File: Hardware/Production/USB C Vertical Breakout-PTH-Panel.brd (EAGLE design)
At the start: 106.7 x 103.4 mm, 586 parts

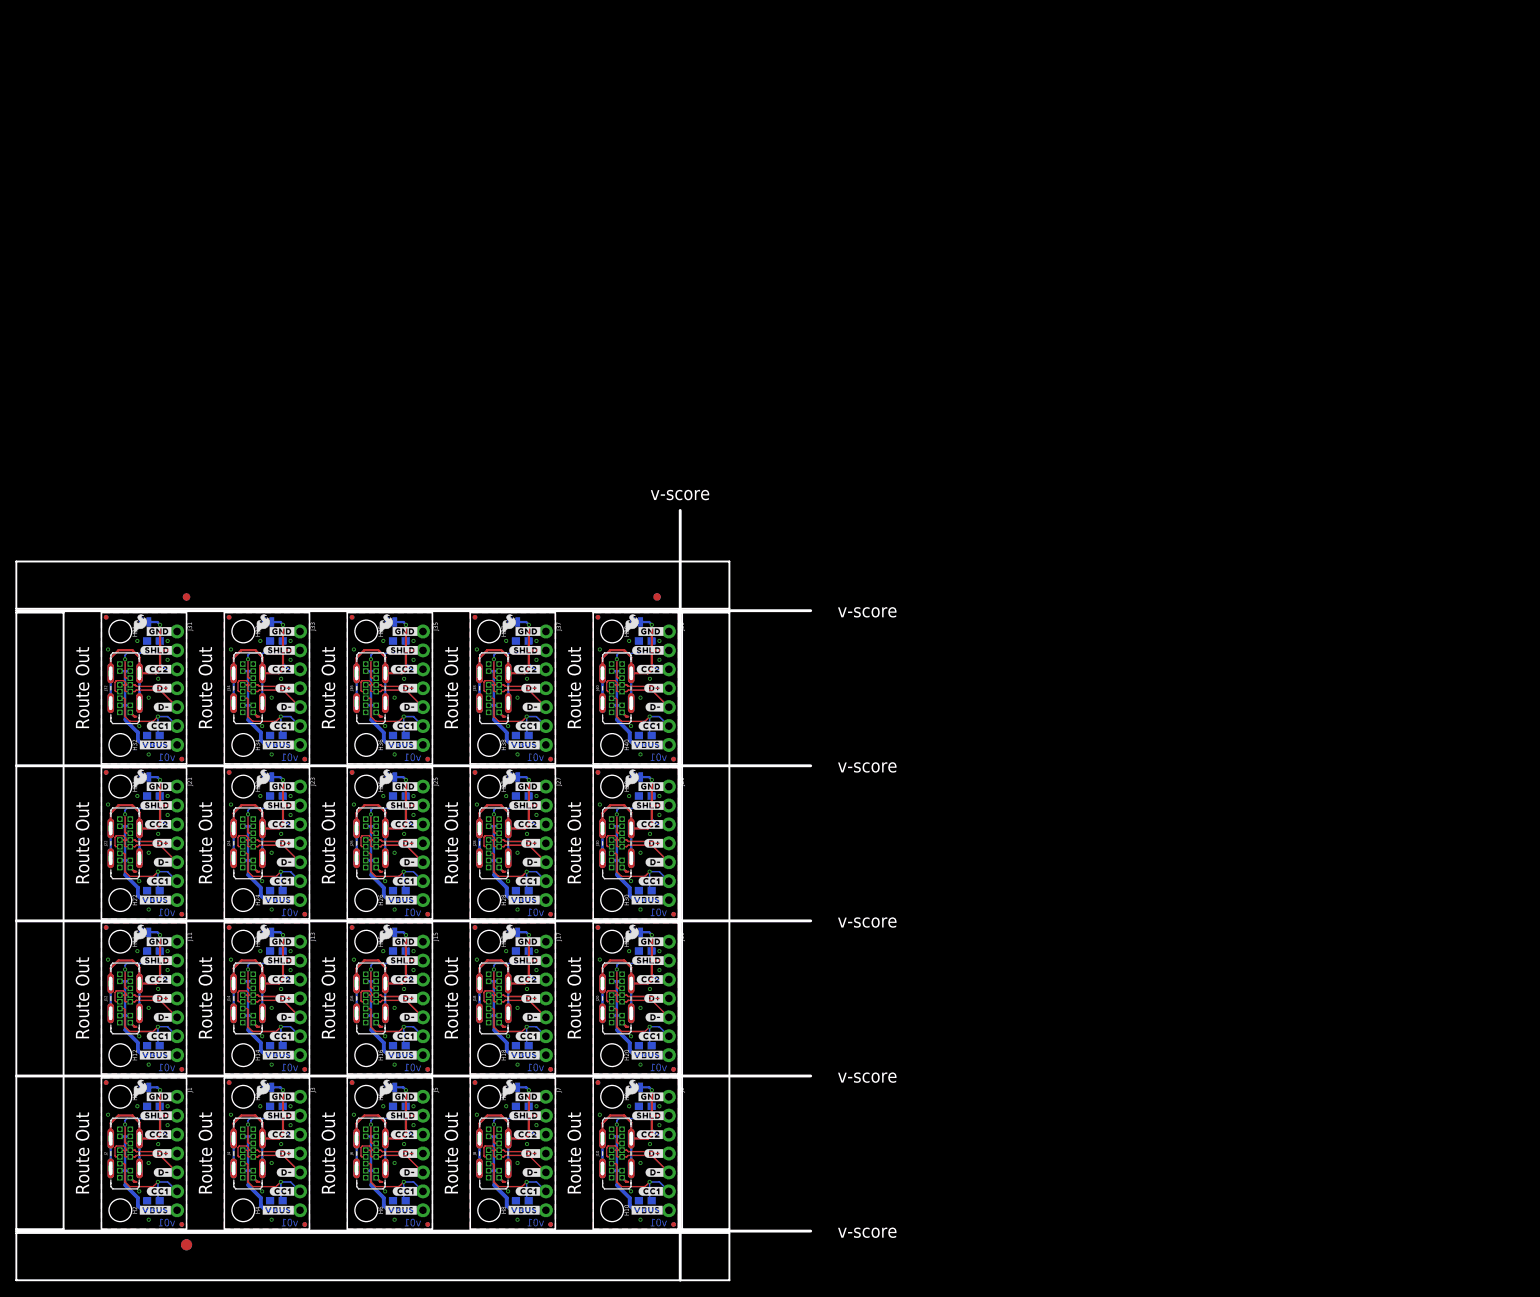
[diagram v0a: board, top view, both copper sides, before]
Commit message: Updates for larger panel size
Updated the design to be a larger panel size for ordering new parts.
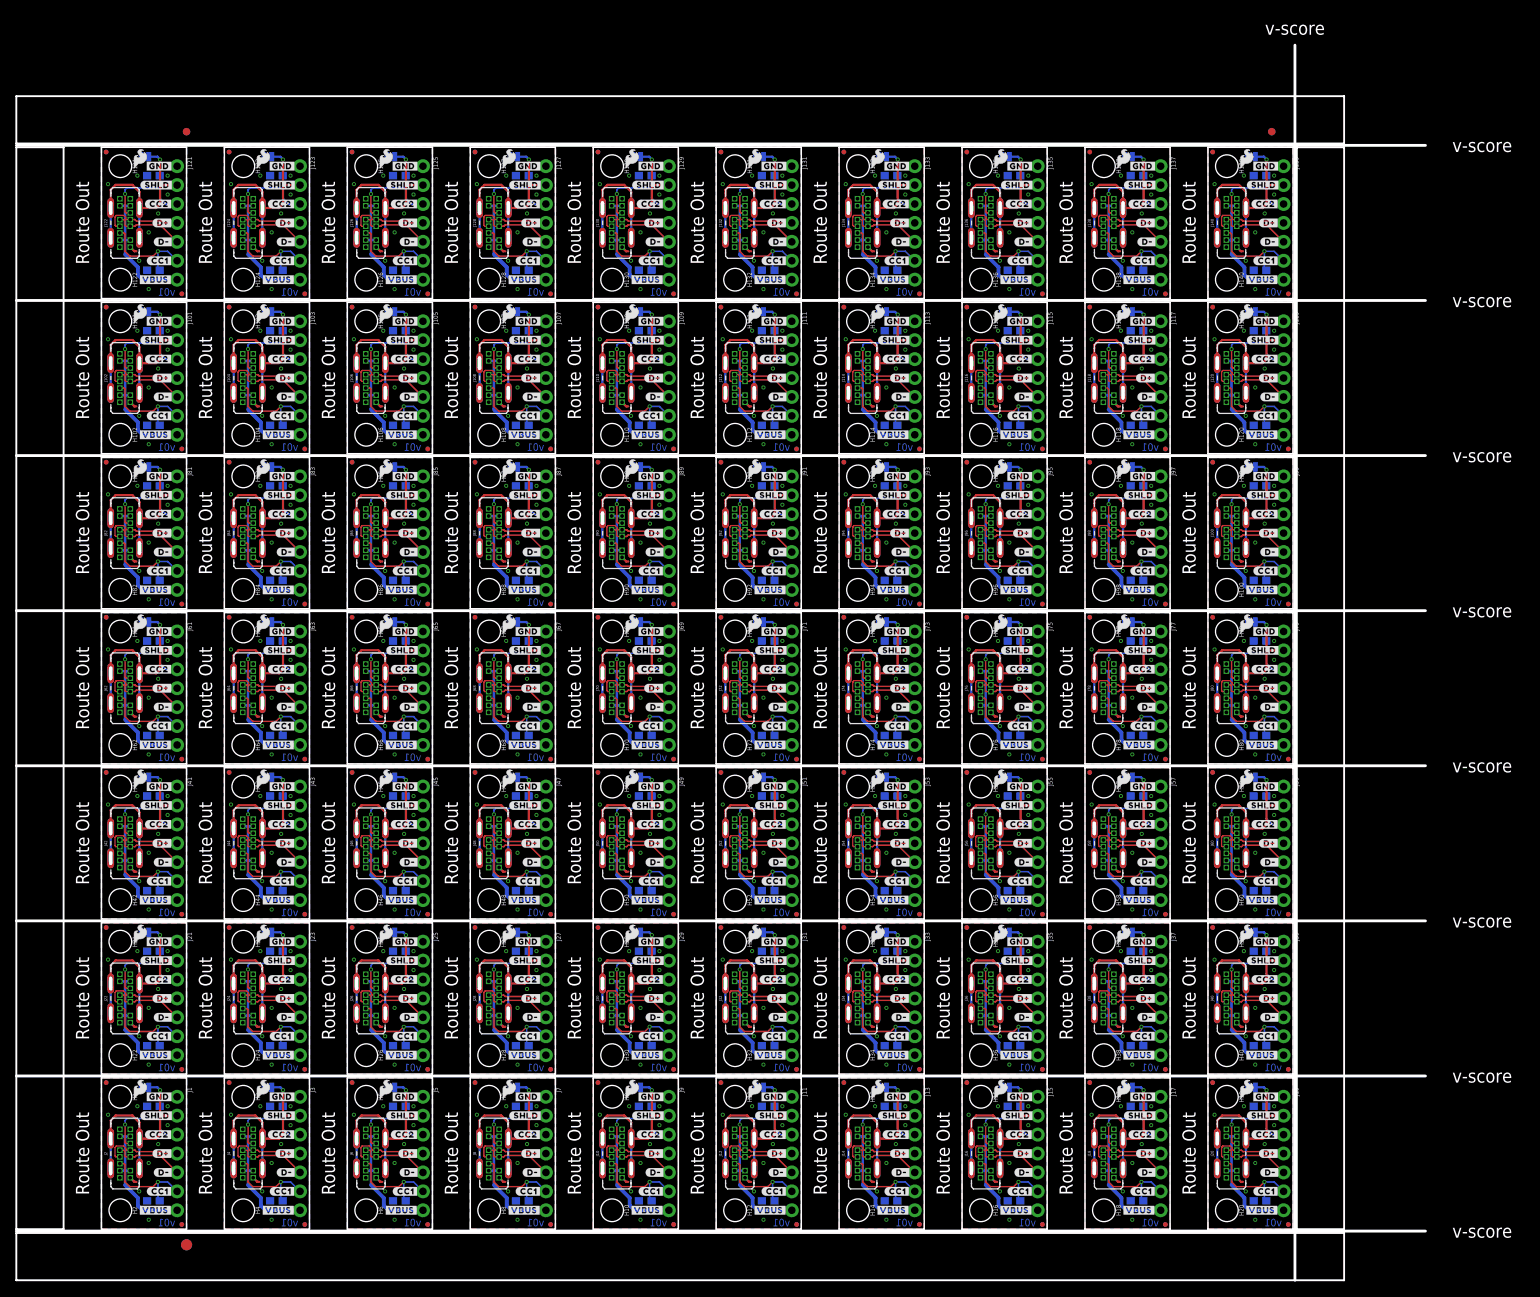
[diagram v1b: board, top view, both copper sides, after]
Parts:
- added FD100, FD101, FD102, FD103, FD104, FD105, FD106, FD107, FD108, FD109, FD110, FD111, FD112, FD113, FD114, FD115, FD116, FD117, FD118, FD119, FD120, FD121, FD122, FD123, FD124, FD125, FD126, FD127, FD128, FD129, FD130, FD131, FD132, FD133, FD134, FD135, FD136, FD137, FD138, FD139, FD140, FD141, FD142, FD143, FD144, FD145, FD146, FD147, FD148, FD149, FD150, FD151, FD152, FD153, FD154, FD155, FD156, FD157, FD158, FD159, FD160, FD161, FD162, FD163, FD164, FD165, FD166, FD167, FD168, FD169, FD170, FD171, FD172, FD173, FD174, FD175, FD176, FD177, FD178, FD179, FD180, FD181, FD182, FD183, FD184, FD185, FD186, FD187, FD188, FD189, FD190, FD191, FD192, FD193, FD194, FD195, FD196, FD197, FD198, FD199, FD200, FD201, FD202, FD203, FD204, FD205, FD206, FD207, FD208, FD209, FD210, FD211, FD212, FD213, FD214, FD215, FD216, FD217, FD218, FD219, FD220, FD221, FD222, FD223, FD224, FD225, FD226, FD227, FD228, FD229, FD230, FD231, FD232, FD233, FD234, FD235, FD236, FD237, FD238, FD239, FD240, FD241, FD242, FD243, FD244, FD245, FD246, FD247, FD248, FD249, FD250, FD251, FD252, FD253, FD254, FD255, FD256, FD257, FD258, FD259, FD260, FD261, FD262, FD263, FD264, FD265, FD266, FD267, FD268, FD269, FD270, FD271, FD272, FD273, FD274, FD275, FD276, FD277, FD278, FD279, FD280, FD81, FD82, FD83, FD84, FD85, FD86, FD87, FD88, FD89, FD90, FD91, FD92, FD93, FD94, FD95, FD96, FD97, FD98, FD99: FIDUCIALUFIDUCIAL, SparkFun-Aesthetics:FIDUCIAL-MICRO
- added H100, H101, H102, H103, H104, H105, H106, H107, H108, H109, H110, H111, H112, H113, H114, H115, H116, H117, H118, H119, H120, H121, H122, H123, H124, H125, H126, H127, H128, H129, H130, H131, H132, H133, H134, H135, H136, H137, H138, H139, H140, H41, H42, H43, H44, H45, H46, H47, H48, H49, H50, H51, H52, H53, H54, H55, H56, H57, H58, H59, H60, H61, H62, H63, H64, H65, H66, H67, H68, H69, H70, H71, H72, H73, H74, H75, H76, H77, H78, H79, H80, H81, H82, H83, H84, H85, H86, H87, H88, H89, H90, H91, H92, H93, H94, H95, H96, H97, H98, H99: STAND-OFFTIGHT, SparkFun-Hardware:STAND-OFF-TIGHT
- added J100, J102, J104, J106, J108, J110, J112, J114, J116, J118, J120, J122, J124, J126, J128, J130, J132, J134, J136, J138, J140, J42, J44, J46, J48, J50, J52, J54, J56, J58, J60, J62, J64, J66, J68, J70, J72, J74, J76, J78, J80, J82, J84, J86, J88, J90, J92, J94, J96, J98: (no value), USB-C_Vertical:USB-C-8P-2LAYER-VERTICAL-PTH
- added J101, J103, J105, J107, J109, J111, J113, J115, J117, J119, J121, J123, J125, J127, J129, J131, J133, J135, J137, J139, J41, J43, J45, J47, J49, J51, J53, J55, J57, J59, J61, J63, J65, J67, J69, J71, J73, J75, J77, J79, J81, J83, J85, J87, J89, J91, J93, J95, J97, J99: (no value), SparkFun-Connectors:1X07_NO_SILK
- added LOGO100, LOGO103, LOGO106, LOGO109, LOGO112, LOGO115, LOGO118, LOGO121, LOGO124, LOGO127, LOGO130, LOGO133, LOGO136, LOGO139, LOGO142, LOGO145, LOGO148, LOGO151, LOGO154, LOGO157, LOGO160, LOGO163, LOGO166, LOGO169, LOGO172, LOGO175, LOGO178, LOGO181, LOGO184, LOGO187, LOGO190, LOGO193, LOGO196, LOGO199, LOGO202, LOGO205, LOGO208, LOGO61, LOGO64, LOGO67, LOGO70, LOGO73, LOGO76, LOGO79, LOGO82, LOGO85, LOGO88, LOGO91, LOGO94, LOGO97: OSHW-LOGOMINI, SparkFun-Aesthetics:OSHW-LOGO-MINI
- added LOGO101, LOGO104, LOGO107, LOGO110, LOGO113, LOGO116, LOGO119, LOGO122, LOGO125, LOGO128, LOGO131, LOGO134, LOGO137, LOGO140, LOGO143, LOGO146, LOGO149, LOGO152, LOGO155, LOGO158, LOGO161, LOGO164, LOGO167, LOGO170, LOGO173, LOGO176, LOGO179, LOGO182, LOGO185, LOGO188, LOGO191, LOGO194, LOGO197, LOGO200, LOGO203, LOGO206, LOGO209, LOGO62, LOGO65, LOGO68, LOGO71, LOGO74, LOGO77, LOGO80, LOGO83, LOGO86, LOGO89, LOGO92, LOGO95, LOGO98: SFE_LOGO_NAME_FLAMEBLANK, SparkFun-Aesthetics:BLANK
- added LOGO102, LOGO105, LOGO108, LOGO111, LOGO114, LOGO117, LOGO120, LOGO123, LOGO126, LOGO129, LOGO132, LOGO135, LOGO138, LOGO141, LOGO144, LOGO147, LOGO150, LOGO153, LOGO156, LOGO159, LOGO162, LOGO165, LOGO168, LOGO171, LOGO174, LOGO177, LOGO180, LOGO183, LOGO186, LOGO189, LOGO192, LOGO195, LOGO198, LOGO201, LOGO204, LOGO207, LOGO210, LOGO63, LOGO66, LOGO69, LOGO72, LOGO75, LOGO78, LOGO81, LOGO84, LOGO87, LOGO90, LOGO93, LOGO96, LOGO99: SFE_LOGO_FLAME.1_INCH, SparkFun-Aesthetics:SFE_LOGO_FLAME_.1
- added R100, R101, R102, R103, R104, R105, R106, R107, R108, R109, R110, R111, R112, R113, R114, R115, R116, R117, R118, R119, R120, R121, R122, R123, R124, R125, R126, R127, R128, R129, R130, R131, R132, R133, R134, R135, R136, R137, R138, R139, R140, R41, R42, R43, R44, R45, R46, R47, R48, R49, R50, R51, R52, R53, R54, R55, R56, R57, R58, R59, R60, R61, R62, R63, R64, R65, R66, R67, R68, R69, R70, R71, R72, R73, R74, R75, R76, R77, R78, R79, R80, R81, R82, R83, R84, R85, R86, R87, R88, R89, R90, R91, R92, R93, R94, R95, R96, R97, R98, R99: 5.1k, SparkFun-Resistors:0603
- added SHLD20, SHLD21, SHLD22, SHLD23, SHLD24, SHLD25, SHLD26, SHLD27, SHLD28, SHLD29, SHLD30, SHLD31, SHLD32, SHLD33, SHLD34, SHLD35, SHLD36, SHLD37, SHLD38, SHLD39, SHLD40, SHLD41, SHLD42, SHLD43, SHLD44, SHLD45, SHLD46, SHLD47, SHLD48, SHLD49, SHLD50, SHLD51, SHLD52, SHLD53, SHLD54, SHLD55, SHLD56, SHLD57, SHLD58, SHLD59, SHLD60, SHLD61, SHLD62, SHLD63, SHLD64, SHLD65, SHLD66, SHLD67, SHLD68, SHLD69: SHLD, SparkFun-Jumpers:SMT-JUMPER_2_NC_TRACE_NO-SILK
- added U$1000, U$1015, U$1030, U$1045, U$310, U$325, U$340, U$355, U$370, U$385, U$400, U$415, U$430, U$445, U$460, U$475, U$490, U$505, U$520, U$535, U$550, U$565, U$580, U$595, U$610, U$625, U$640, U$655, U$670, U$685, U$700, U$715, U$730, U$745, U$760, U$775, U$790, U$805, U$820, U$835, U$850, U$865, U$880, U$895, U$910, U$925, U$940, U$955, U$970, U$985: (no value), output:#SHLD#8
- added U$1001, U$1016, U$1031, U$1046, U$311, U$326, U$341, U$356, U$371, U$386, U$401, U$416, U$431, U$446, U$461, U$476, U$491, U$506, U$521, U$536, U$551, U$566, U$581, U$596, U$611, U$626, U$641, U$656, U$671, U$686, U$701, U$716, U$731, U$746, U$761, U$776, U$791, U$806, U$821, U$836, U$851, U$866, U$881, U$896, U$911, U$926, U$941, U$956, U$971, U$986: (no value), output:#CC2#9
- added U$1002, U$1017, U$1032, U$1047, U$312, U$327, U$342, U$357, U$372, U$387, U$402, U$417, U$432, U$447, U$462, U$477, U$492, U$507, U$522, U$537, U$552, U$567, U$582, U$597, U$612, U$627, U$642, U$657, U$672, U$687, U$702, U$717, U$732, U$747, U$762, U$777, U$792, U$807, U$822, U$837, U$852, U$867, U$882, U$897, U$912, U$927, U$942, U$957, U$972, U$987: (no value), output:#D##9
- added U$1003, U$1018, U$1033, U$1048, U$313, U$328, U$343, U$358, U$373, U$388, U$403, U$418, U$433, U$448, U$463, U$478, U$493, U$508, U$523, U$538, U$553, U$568, U$583, U$598, U$613, U$628, U$643, U$658, U$673, U$688, U$703, U$718, U$733, U$748, U$763, U$778, U$793, U$808, U$823, U$838, U$853, U$868, U$883, U$898, U$913, U$928, U$943, U$958, U$973, U$988: (no value), output:#D##10
- added U$1004, U$1019, U$1034, U$1049, U$314, U$329, U$344, U$359, U$374, U$389, U$404, U$419, U$434, U$449, U$464, U$479, U$494, U$509, U$524, U$539, U$554, U$569, U$584, U$599, U$614, U$629, U$644, U$659, U$674, U$689, U$704, U$719, U$734, U$749, U$764, U$779, U$794, U$809, U$824, U$839, U$854, U$869, U$884, U$899, U$914, U$929, U$944, U$959, U$974, U$989: (no value), output:#CC1#11
- added U$1005, U$1020, U$1035, U$1050, U$315, U$330, U$345, U$360, U$375, U$390, U$405, U$420, U$435, U$450, U$465, U$480, U$495, U$510, U$525, U$540, U$555, U$570, U$585, U$600, U$615, U$630, U$645, U$660, U$675, U$690, U$705, U$720, U$735, U$750, U$765, U$780, U$795, U$810, U$825, U$840, U$855, U$870, U$885, U$900, U$915, U$930, U$945, U$960, U$975, U$990: (no value), output:SHLD0
- added U$1006, U$1021, U$1036, U$301, U$316, U$331, U$346, U$361, U$376, U$391, U$406, U$421, U$436, U$451, U$466, U$481, U$496, U$511, U$526, U$541, U$556, U$571, U$586, U$601, U$616, U$631, U$646, U$661, U$676, U$691, U$706, U$721, U$736, U$751, U$766, U$781, U$796, U$811, U$826, U$841, U$856, U$871, U$886, U$901, U$916, U$931, U$946, U$961, U$976, U$991: (no value), output:#CC2#0
- added U$1007, U$1022, U$1037, U$302, U$317, U$332, U$347, U$362, U$377, U$392, U$407, U$422, U$437, U$452, U$467, U$482, U$497, U$512, U$527, U$542, U$557, U$572, U$587, U$602, U$617, U$632, U$647, U$662, U$677, U$692, U$707, U$722, U$737, U$752, U$767, U$782, U$797, U$812, U$827, U$842, U$857, U$872, U$887, U$902, U$917, U$932, U$947, U$962, U$977, U$992: (no value), output:#D##3
- added U$1008, U$1023, U$1038, U$303, U$318, U$333, U$348, U$363, U$378, U$393, U$408, U$423, U$438, U$453, U$468, U$483, U$498, U$513, U$528, U$543, U$558, U$573, U$588, U$603, U$618, U$633, U$648, U$663, U$678, U$693, U$708, U$723, U$738, U$753, U$768, U$783, U$798, U$813, U$828, U$843, U$858, U$873, U$888, U$903, U$918, U$933, U$948, U$963, U$978, U$993: (no value), output:#D##4
- added U$1009, U$1024, U$1039, U$304, U$319, U$334, U$349, U$364, U$379, U$394, U$409, U$424, U$439, U$454, U$469, U$484, U$499, U$514, U$529, U$544, U$559, U$574, U$589, U$604, U$619, U$634, U$649, U$664, U$679, U$694, U$709, U$724, U$739, U$754, U$769, U$784, U$799, U$814, U$829, U$844, U$859, U$874, U$889, U$904, U$919, U$934, U$949, U$964, U$979, U$994: (no value), output:#CC1#5
- added U$1010, U$1025, U$1040, U$305, U$320, U$335, U$350, U$365, U$380, U$395, U$410, U$425, U$440, U$455, U$470, U$485, U$500, U$515, U$530, U$545, U$560, U$575, U$590, U$605, U$620, U$635, U$650, U$665, U$680, U$695, U$710, U$725, U$740, U$755, U$770, U$785, U$800, U$815, U$830, U$845, U$860, U$875, U$890, U$905, U$920, U$935, U$950, U$965, U$980, U$995: (no value), output:#SHLD#5
- added U$1011, U$1014, U$1026, U$1029, U$1041, U$1044, U$306, U$309, U$321, U$324, U$336, U$339, U$351, U$354, U$366, U$369, U$381, U$384, U$396, U$399, U$411, U$414, U$426, U$429, U$441, U$444, U$456, U$459, U$471, U$474, U$486, U$489, U$501, U$504, U$516, U$519, U$531, U$534, U$546, U$549, U$561, U$564, U$576, U$579, U$591, U$594, U$606, U$609, U$621, U$624, U$636, U$639, U$651, U$654, U$666, U$669, U$681, U$684, U$696, U$699, U$711, U$714, U$726, U$729, U$741, U$744, U$756, U$759, U$771, U$774, U$786, U$789, U$801, U$804, U$816, U$819, U$831, U$834, U$846, U$849, U$861, U$864, U$876, U$879, U$891, U$894, U$906, U$909, U$921, U$924, U$936, U$939, U$951, U$954, U$966, U$969, U$981, U$984, U$996, U$999: (no value), output:#GND#6
- added U$1012, U$1013, U$1027, U$1028, U$1042, U$1043, U$307, U$308, U$322, U$323, U$337, U$338, U$352, U$353, U$367, U$368, U$382, U$383, U$397, U$398, U$412, U$413, U$427, U$428, U$442, U$443, U$457, U$458, U$472, U$473, U$487, U$488, U$502, U$503, U$517, U$518, U$532, U$533, U$547, U$548, U$562, U$563, U$577, U$578, U$592, U$593, U$607, U$608, U$622, U$623, U$637, U$638, U$652, U$653, U$667, U$668, U$682, U$683, U$697, U$698, U$712, U$713, U$727, U$728, U$742, U$743, U$757, U$758, U$772, U$773, U$787, U$788, U$802, U$803, U$817, U$818, U$832, U$833, U$847, U$848, U$862, U$863, U$877, U$878, U$892, U$893, U$907, U$908, U$922, U$923, U$937, U$938, U$952, U$953, U$967, U$968, U$982, U$983, U$997, U$998: (no value), output:#VBUS#7
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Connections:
- new net CC100: J100.B5, J99.3, R100.2
- new net CC101: J101.6, J102.A5, R101.2
- new net CC102: J101.3, J102.B5, R102.2
- new net CC103: J103.6, J104.A5, R103.2
- new net CC104: J103.3, J104.B5, R104.2
- new net CC105: J105.6, J106.A5, R105.2
- new net CC106: J105.3, J106.B5, R106.2
- new net CC107: J107.6, J108.A5, R107.2
- new net CC108: J107.3, J108.B5, R108.2
- new net CC109: J109.6, J110.A5, R109.2
- new net CC110: J109.3, J110.B5, R110.2
- new net CC111: J111.6, J112.A5, R111.2
- new net CC112: J111.3, J112.B5, R112.2
- new net CC113: J113.6, J114.A5, R113.2
- new net CC114: J113.3, J114.B5, R114.2
- new net CC115: J115.6, J116.A5, R115.2
- new net CC116: J115.3, J116.B5, R116.2
- new net CC117: J117.6, J118.A5, R117.2
- new net CC118: J117.3, J118.B5, R118.2
- new net CC119: J119.6, J120.A5, R119.2
- new net CC120: J119.3, J120.B5, R120.2
- new net CC121: J121.6, J122.A5, R121.2
- new net CC122: J121.3, J122.B5, R122.2
- new net CC123: J123.6, J124.A5, R123.2
- new net CC124: J123.3, J124.B5, R124.2
- new net CC125: J125.6, J126.A5, R125.2
- new net CC126: J125.3, J126.B5, R126.2
- new net CC127: J127.6, J128.A5, R127.2
- new net CC128: J127.3, J128.B5, R128.2
- new net CC129: J129.6, J130.A5, R129.2
- new net CC130: J129.3, J130.B5, R130.2
- new net CC131: J131.6, J132.A5, R131.2
- new net CC132: J131.3, J132.B5, R132.2
- new net CC133: J133.6, J134.A5, R133.2
- new net CC134: J133.3, J134.B5, R134.2
- new net CC135: J135.6, J136.A5, R135.2
- new net CC136: J135.3, J136.B5, R136.2
- new net CC137: J137.6, J138.A5, R137.2
- new net CC138: J137.3, J138.B5, R138.2
- new net CC139: J139.6, J140.A5, R139.2
- new net CC140: J139.3, J140.B5, R140.2
- new net CC41: J41.6, J42.A5, R41.2
- new net CC42: J41.3, J42.B5, R42.2
- new net CC43: J43.6, J44.A5, R43.2
- new net CC44: J43.3, J44.B5, R44.2
- new net CC45: J45.6, J46.A5, R45.2
- new net CC46: J45.3, J46.B5, R46.2
- new net CC47: J47.6, J48.A5, R47.2
- new net CC48: J47.3, J48.B5, R48.2
- new net CC49: J49.6, J50.A5, R49.2
- new net CC50: J49.3, J50.B5, R50.2
- new net CC51: J51.6, J52.A5, R51.2
- new net CC52: J51.3, J52.B5, R52.2
- new net CC53: J53.6, J54.A5, R53.2
- new net CC54: J53.3, J54.B5, R54.2
- new net CC55: J55.6, J56.A5, R55.2
- new net CC56: J55.3, J56.B5, R56.2
- new net CC57: J57.6, J58.A5, R57.2
- new net CC58: J57.3, J58.B5, R58.2
- new net CC59: J59.6, J60.A5, R59.2
- new net CC60: J59.3, J60.B5, R60.2
- new net CC61: J61.6, J62.A5, R61.2
- new net CC62: J61.3, J62.B5, R62.2
- new net CC63: J63.6, J64.A5, R63.2
- new net CC64: J63.3, J64.B5, R64.2
- new net CC65: J65.6, J66.A5, R65.2
- new net CC66: J65.3, J66.B5, R66.2
- new net CC67: J67.6, J68.A5, R67.2
- new net CC68: J67.3, J68.B5, R68.2
- new net CC69: J69.6, J70.A5, R69.2
- new net CC70: J69.3, J70.B5, R70.2
- new net CC71: J71.6, J72.A5, R71.2
- new net CC72: J71.3, J72.B5, R72.2
- new net CC73: J73.6, J74.A5, R73.2
- new net CC74: J73.3, J74.B5, R74.2
- new net CC75: J75.6, J76.A5, R75.2
- new net CC76: J75.3, J76.B5, R76.2
- new net CC77: J77.6, J78.A5, R77.2
- new net CC78: J77.3, J78.B5, R78.2
- new net CC79: J79.6, J80.A5, R79.2
- new net CC80: J79.3, J80.B5, R80.2
- new net CC81: J81.6, J82.A5, R81.2
- new net CC82: J81.3, J82.B5, R82.2
- new net CC83: J83.6, J84.A5, R83.2
- new net CC84: J83.3, J84.B5, R84.2
- new net CC85: J85.6, J86.A5, R85.2
- new net CC86: J85.3, J86.B5, R86.2
- new net CC87: J87.6, J88.A5, R87.2
- new net CC88: J87.3, J88.B5, R88.2
- new net CC89: J89.6, J90.A5, R89.2
- new net CC90: J89.3, J90.B5, R90.2
- new net CC91: J91.6, J92.A5, R91.2
- new net CC92: J91.3, J92.B5, R92.2
- new net CC93: J93.6, J94.A5, R93.2
- new net CC94: J93.3, J94.B5, R94.2
- new net CC95: J95.6, J96.A5, R95.2
- new net CC96: J95.3, J96.B5, R96.2
- new net CC97: J97.6, J98.A5, R97.2
- new net CC98: J97.3, J98.B5, R98.2
- new net CC99: J100.A5, J99.6, R99.2
- new net D+20: J41.4, J42.A6, J42.B6
- new net D+21: J43.4, J44.A6, J44.B6
- new net D+22: J45.4, J46.A6, J46.B6
- new net D+23: J47.4, J48.A6, J48.B6
- new net D+24: J49.4, J50.A6, J50.B6
- new net D+25: J51.4, J52.A6, J52.B6
- new net D+26: J53.4, J54.A6, J54.B6
- new net D+27: J55.4, J56.A6, J56.B6
- new net D+28: J57.4, J58.A6, J58.B6
- new net D+29: J59.4, J60.A6, J60.B6
- new net D+30: J61.4, J62.A6, J62.B6
- new net D+31: J63.4, J64.A6, J64.B6
- new net D+32: J65.4, J66.A6, J66.B6
- new net D+33: J67.4, J68.A6, J68.B6
- new net D+34: J69.4, J70.A6, J70.B6
- new net D+35: J71.4, J72.A6, J72.B6
- new net D+36: J73.4, J74.A6, J74.B6
- new net D+37: J75.4, J76.A6, J76.B6
- new net D+38: J77.4, J78.A6, J78.B6
- new net D+39: J79.4, J80.A6, J80.B6
- new net D+40: J81.4, J82.A6, J82.B6
- new net D+41: J83.4, J84.A6, J84.B6
- new net D+42: J85.4, J86.A6, J86.B6
- new net D+43: J87.4, J88.A6, J88.B6
- new net D+44: J89.4, J90.A6, J90.B6
- new net D+45: J91.4, J92.A6, J92.B6
- new net D+46: J93.4, J94.A6, J94.B6
- new net D+47: J95.4, J96.A6, J96.B6
- new net D+48: J97.4, J98.A6, J98.B6
- new net D+49: J100.A6, J100.B6, J99.4
- new net D+50: J101.4, J102.A6, J102.B6
- new net D+51: J103.4, J104.A6, J104.B6
- new net D+52: J105.4, J106.A6, J106.B6
- new net D+53: J107.4, J108.A6, J108.B6
- new net D+54: J109.4, J110.A6, J110.B6
- new net D+55: J111.4, J112.A6, J112.B6
- new net D+56: J113.4, J114.A6, J114.B6
- new net D+57: J115.4, J116.A6, J116.B6
- new net D+58: J117.4, J118.A6, J118.B6
- new net D+59: J119.4, J120.A6, J120.B6
- new net D+60: J121.4, J122.A6, J122.B6
- new net D+61: J123.4, J124.A6, J124.B6
- new net D+62: J125.4, J126.A6, J126.B6
- new net D+63: J127.4, J128.A6, J128.B6
- new net D+64: J129.4, J130.A6, J130.B6
- new net D+65: J131.4, J132.A6, J132.B6
- new net D+66: J133.4, J134.A6, J134.B6
- new net D+67: J135.4, J136.A6, J136.B6
- new net D+68: J137.4, J138.A6, J138.B6
- new net D+69: J139.4, J140.A6, J140.B6
- new net D-20: J41.5, J42.A7, J42.B7
- new net D-21: J43.5, J44.A7, J44.B7
- new net D-22: J45.5, J46.A7, J46.B7
- new net D-23: J47.5, J48.A7, J48.B7
- new net D-24: J49.5, J50.A7, J50.B7
- new net D-25: J51.5, J52.A7, J52.B7
- new net D-26: J53.5, J54.A7, J54.B7
- new net D-27: J55.5, J56.A7, J56.B7
- new net D-28: J57.5, J58.A7, J58.B7
- new net D-29: J59.5, J60.A7, J60.B7
- new net D-30: J61.5, J62.A7, J62.B7
- new net D-31: J63.5, J64.A7, J64.B7
- new net D-32: J65.5, J66.A7, J66.B7
- new net D-33: J67.5, J68.A7, J68.B7
- new net D-34: J69.5, J70.A7, J70.B7
- new net D-35: J71.5, J72.A7, J72.B7
- new net D-36: J73.5, J74.A7, J74.B7
- new net D-37: J75.5, J76.A7, J76.B7
- new net D-38: J77.5, J78.A7, J78.B7
- new net D-39: J79.5, J80.A7, J80.B7
- new net D-40: J81.5, J82.A7, J82.B7
- new net D-41: J83.5, J84.A7, J84.B7
- new net D-42: J85.5, J86.A7, J86.B7
- new net D-43: J87.5, J88.A7, J88.B7
- new net D-44: J89.5, J90.A7, J90.B7
- new net D-45: J91.5, J92.A7, J92.B7
- new net D-46: J93.5, J94.A7, J94.B7
- new net D-47: J95.5, J96.A7, J96.B7
- new net D-48: J97.5, J98.A7, J98.B7
- new net D-49: J100.A7, J100.B7, J99.5
- new net D-50: J101.5, J102.A7, J102.B7
- new net D-51: J103.5, J104.A7, J104.B7
- new net D-52: J105.5, J106.A7, J106.B7
- new net D-53: J107.5, J108.A7, J108.B7
- new net D-54: J109.5, J110.A7, J110.B7
- new net D-55: J111.5, J112.A7, J112.B7
- new net D-56: J113.5, J114.A7, J114.B7
- new net D-57: J115.5, J116.A7, J116.B7
- new net D-58: J117.5, J118.A7, J118.B7
- new net D-59: J119.5, J120.A7, J120.B7
- new net D-60: J121.5, J122.A7, J122.B7
- new net D-61: J123.5, J124.A7, J124.B7
- new net D-62: J125.5, J126.A7, J126.B7
- new net D-63: J127.5, J128.A7, J128.B7
- new net D-64: J129.5, J130.A7, J130.B7
- new net D-65: J131.5, J132.A7, J132.B7
- new net D-66: J133.5, J134.A7, J134.B7
- new net D-67: J135.5, J136.A7, J136.B7
- new net D-68: J137.5, J138.A7, J138.B7
- new net D-69: J139.5, J140.A7, J140.B7
- new net GND20: J41.1, J42.A1, J42.A12, J42.B1, J42.B12, R41.1, R42.1, SHLD20.1
- new net GND21: J43.1, J44.A1, J44.A12, J44.B1, J44.B12, R43.1, R44.1, SHLD21.1
- new net GND22: J45.1, J46.A1, J46.A12, J46.B1, J46.B12, R45.1, R46.1, SHLD22.1
- new net GND23: J47.1, J48.A1, J48.A12, J48.B1, J48.B12, R47.1, R48.1, SHLD23.1
- new net GND24: J49.1, J50.A1, J50.A12, J50.B1, J50.B12, R49.1, R50.1, SHLD24.1
- new net GND25: J51.1, J52.A1, J52.A12, J52.B1, J52.B12, R51.1, R52.1, SHLD25.1
- new net GND26: J53.1, J54.A1, J54.A12, J54.B1, J54.B12, R53.1, R54.1, SHLD26.1
- new net GND27: J55.1, J56.A1, J56.A12, J56.B1, J56.B12, R55.1, R56.1, SHLD27.1
- new net GND28: J57.1, J58.A1, J58.A12, J58.B1, J58.B12, R57.1, R58.1, SHLD28.1
- new net GND29: J59.1, J60.A1, J60.A12, J60.B1, J60.B12, R59.1, R60.1, SHLD29.1
- new net GND30: J61.1, J62.A1, J62.A12, J62.B1, J62.B12, R61.1, R62.1, SHLD30.1
- new net GND31: J63.1, J64.A1, J64.A12, J64.B1, J64.B12, R63.1, R64.1, SHLD31.1
- new net GND32: J65.1, J66.A1, J66.A12, J66.B1, J66.B12, R65.1, R66.1, SHLD32.1
- new net GND33: J67.1, J68.A1, J68.A12, J68.B1, J68.B12, R67.1, R68.1, SHLD33.1
- new net GND34: J69.1, J70.A1, J70.A12, J70.B1, J70.B12, R69.1, R70.1, SHLD34.1
- new net GND35: J71.1, J72.A1, J72.A12, J72.B1, J72.B12, R71.1, R72.1, SHLD35.1
- new net GND36: J73.1, J74.A1, J74.A12, J74.B1, J74.B12, R73.1, R74.1, SHLD36.1
- new net GND37: J75.1, J76.A1, J76.A12, J76.B1, J76.B12, R75.1, R76.1, SHLD37.1
- new net GND38: J77.1, J78.A1, J78.A12, J78.B1, J78.B12, R77.1, R78.1, SHLD38.1
- new net GND39: J79.1, J80.A1, J80.A12, J80.B1, J80.B12, R79.1, R80.1, SHLD39.1
- new net GND40: J81.1, J82.A1, J82.A12, J82.B1, J82.B12, R81.1, R82.1, SHLD40.1
- new net GND41: J83.1, J84.A1, J84.A12, J84.B1, J84.B12, R83.1, R84.1, SHLD41.1
- new net GND42: J85.1, J86.A1, J86.A12, J86.B1, J86.B12, R85.1, R86.1, SHLD42.1
- new net GND43: J87.1, J88.A1, J88.A12, J88.B1, J88.B12, R87.1, R88.1, SHLD43.1
- new net GND44: J89.1, J90.A1, J90.A12, J90.B1, J90.B12, R89.1, R90.1, SHLD44.1
- new net GND45: J91.1, J92.A1, J92.A12, J92.B1, J92.B12, R91.1, R92.1, SHLD45.1
- new net GND46: J93.1, J94.A1, J94.A12, J94.B1, J94.B12, R93.1, R94.1, SHLD46.1
- new net GND47: J95.1, J96.A1, J96.A12, J96.B1, J96.B12, R95.1, R96.1, SHLD47.1
- new net GND48: J97.1, J98.A1, J98.A12, J98.B1, J98.B12, R97.1, R98.1, SHLD48.1
- new net GND49: J100.A1, J100.A12, J100.B1, J100.B12, J99.1, R100.1, R99.1, SHLD49.1
- new net GND50: J101.1, J102.A1, J102.A12, J102.B1, J102.B12, R101.1, R102.1, SHLD50.1
- new net GND51: J103.1, J104.A1, J104.A12, J104.B1, J104.B12, R103.1, R104.1, SHLD51.1
- new net GND52: J105.1, J106.A1, J106.A12, J106.B1, J106.B12, R105.1, R106.1, SHLD52.1
- new net GND53: J107.1, J108.A1, J108.A12, J108.B1, J108.B12, R107.1, R108.1, SHLD53.1
- new net GND54: J109.1, J110.A1, J110.A12, J110.B1, J110.B12, R109.1, R110.1, SHLD54.1
- new net GND55: J111.1, J112.A1, J112.A12, J112.B1, J112.B12, R111.1, R112.1, SHLD55.1
- new net GND56: J113.1, J114.A1, J114.A12, J114.B1, J114.B12, R113.1, R114.1, SHLD56.1
- new net GND57: J115.1, J116.A1, J116.A12, J116.B1, J116.B12, R115.1, R116.1, SHLD57.1
- new net GND58: J117.1, J118.A1, J118.A12, J118.B1, J118.B12, R117.1, R118.1, SHLD58.1
- new net GND59: J119.1, J120.A1, J120.A12, J120.B1, J120.B12, R119.1, R120.1, SHLD59.1
- new net GND60: J121.1, J122.A1, J122.A12, J122.B1, J122.B12, R121.1, R122.1, SHLD60.1
- new net GND61: J123.1, J124.A1, J124.A12, J124.B1, J124.B12, R123.1, R124.1, SHLD61.1
- new net GND62: J125.1, J126.A1, J126.A12, J126.B1, J126.B12, R125.1, R126.1, SHLD62.1
- new net GND63: J127.1, J128.A1, J128.A12, J128.B1, J128.B12, R127.1, R128.1, SHLD63.1
- new net GND64: J129.1, J130.A1, J130.A12, J130.B1, J130.B12, R129.1, R130.1, SHLD64.1
- new net GND65: J131.1, J132.A1, J132.A12, J132.B1, J132.B12, R131.1, R132.1, SHLD65.1
- new net GND66: J133.1, J134.A1, J134.A12, J134.B1, J134.B12, R133.1, R134.1, SHLD66.1
- new net GND67: J135.1, J136.A1, J136.A12, J136.B1, J136.B12, R135.1, R136.1, SHLD67.1
- new net GND68: J137.1, J138.A1, J138.A12, J138.B1, J138.B12, R137.1, R138.1, SHLD68.1
- new net GND69: J139.1, J140.A1, J140.A12, J140.B1, J140.B12, R139.1, R140.1, SHLD69.1
- new net SHLD20: J41.2, J42.SHLD1, J42.SHLD2, J42.SHLD3, J42.SHLD4, SHLD20.2
- new net SHLD21: J43.2, J44.SHLD1, J44.SHLD2, J44.SHLD3, J44.SHLD4, SHLD21.2
- new net SHLD22: J45.2, J46.SHLD1, J46.SHLD2, J46.SHLD3, J46.SHLD4, SHLD22.2
- new net SHLD23: J47.2, J48.SHLD1, J48.SHLD2, J48.SHLD3, J48.SHLD4, SHLD23.2
- new net SHLD24: J49.2, J50.SHLD1, J50.SHLD2, J50.SHLD3, J50.SHLD4, SHLD24.2
- new net SHLD25: J51.2, J52.SHLD1, J52.SHLD2, J52.SHLD3, J52.SHLD4, SHLD25.2
- new net SHLD26: J53.2, J54.SHLD1, J54.SHLD2, J54.SHLD3, J54.SHLD4, SHLD26.2
- new net SHLD27: J55.2, J56.SHLD1, J56.SHLD2, J56.SHLD3, J56.SHLD4, SHLD27.2
- new net SHLD28: J57.2, J58.SHLD1, J58.SHLD2, J58.SHLD3, J58.SHLD4, SHLD28.2
- new net SHLD29: J59.2, J60.SHLD1, J60.SHLD2, J60.SHLD3, J60.SHLD4, SHLD29.2
- new net SHLD30: J61.2, J62.SHLD1, J62.SHLD2, J62.SHLD3, J62.SHLD4, SHLD30.2
- new net SHLD31: J63.2, J64.SHLD1, J64.SHLD2, J64.SHLD3, J64.SHLD4, SHLD31.2
- new net SHLD32: J65.2, J66.SHLD1, J66.SHLD2, J66.SHLD3, J66.SHLD4, SHLD32.2
- new net SHLD33: J67.2, J68.SHLD1, J68.SHLD2, J68.SHLD3, J68.SHLD4, SHLD33.2
- new net SHLD34: J69.2, J70.SHLD1, J70.SHLD2, J70.SHLD3, J70.SHLD4, SHLD34.2
- new net SHLD35: J71.2, J72.SHLD1, J72.SHLD2, J72.SHLD3, J72.SHLD4, SHLD35.2
- new net SHLD36: J73.2, J74.SHLD1, J74.SHLD2, J74.SHLD3, J74.SHLD4, SHLD36.2
- new net SHLD37: J75.2, J76.SHLD1, J76.SHLD2, J76.SHLD3, J76.SHLD4, SHLD37.2
- new net SHLD38: J77.2, J78.SHLD1, J78.SHLD2, J78.SHLD3, J78.SHLD4, SHLD38.2
- new net SHLD39: J79.2, J80.SHLD1, J80.SHLD2, J80.SHLD3, J80.SHLD4, SHLD39.2
- new net SHLD40: J81.2, J82.SHLD1, J82.SHLD2, J82.SHLD3, J82.SHLD4, SHLD40.2
- new net SHLD41: J83.2, J84.SHLD1, J84.SHLD2, J84.SHLD3, J84.SHLD4, SHLD41.2
- new net SHLD42: J85.2, J86.SHLD1, J86.SHLD2, J86.SHLD3, J86.SHLD4, SHLD42.2
- new net SHLD43: J87.2, J88.SHLD1, J88.SHLD2, J88.SHLD3, J88.SHLD4, SHLD43.2
- new net SHLD44: J89.2, J90.SHLD1, J90.SHLD2, J90.SHLD3, J90.SHLD4, SHLD44.2
- new net SHLD45: J91.2, J92.SHLD1, J92.SHLD2, J92.SHLD3, J92.SHLD4, SHLD45.2
- new net SHLD46: J93.2, J94.SHLD1, J94.SHLD2, J94.SHLD3, J94.SHLD4, SHLD46.2
- new net SHLD47: J95.2, J96.SHLD1, J96.SHLD2, J96.SHLD3, J96.SHLD4, SHLD47.2
- new net SHLD48: J97.2, J98.SHLD1, J98.SHLD2, J98.SHLD3, J98.SHLD4, SHLD48.2
- new net SHLD49: J100.SHLD1, J100.SHLD2, J100.SHLD3, J100.SHLD4, J99.2, SHLD49.2
- new net SHLD50: J101.2, J102.SHLD1, J102.SHLD2, J102.SHLD3, J102.SHLD4, SHLD50.2
- new net SHLD51: J103.2, J104.SHLD1, J104.SHLD2, J104.SHLD3, J104.SHLD4, SHLD51.2
- new net SHLD52: J105.2, J106.SHLD1, J106.SHLD2, J106.SHLD3, J106.SHLD4, SHLD52.2
- new net SHLD53: J107.2, J108.SHLD1, J108.SHLD2, J108.SHLD3, J108.SHLD4, SHLD53.2
- new net SHLD54: J109.2, J110.SHLD1, J110.SHLD2, J110.SHLD3, J110.SHLD4, SHLD54.2
- new net SHLD55: J111.2, J112.SHLD1, J112.SHLD2, J112.SHLD3, J112.SHLD4, SHLD55.2
- new net SHLD56: J113.2, J114.SHLD1, J114.SHLD2, J114.SHLD3, J114.SHLD4, SHLD56.2
- new net SHLD57: J115.2, J116.SHLD1, J116.SHLD2, J116.SHLD3, J116.SHLD4, SHLD57.2
- new net SHLD58: J117.2, J118.SHLD1, J118.SHLD2, J118.SHLD3, J118.SHLD4, SHLD58.2
- new net SHLD59: J119.2, J120.SHLD1, J120.SHLD2, J120.SHLD3, J120.SHLD4, SHLD59.2
- new net SHLD60: J121.2, J122.SHLD1, J122.SHLD2, J122.SHLD3, J122.SHLD4, SHLD60.2
- new net SHLD61: J123.2, J124.SHLD1, J124.SHLD2, J124.SHLD3, J124.SHLD4, SHLD61.2
- new net SHLD62: J125.2, J126.SHLD1, J126.SHLD2, J126.SHLD3, J126.SHLD4, SHLD62.2
- new net SHLD63: J127.2, J128.SHLD1, J128.SHLD2, J128.SHLD3, J128.SHLD4, SHLD63.2
- new net SHLD64: J129.2, J130.SHLD1, J130.SHLD2, J130.SHLD3, J130.SHLD4, SHLD64.2
- new net SHLD65: J131.2, J132.SHLD1, J132.SHLD2, J132.SHLD3, J132.SHLD4, SHLD65.2
- new net SHLD66: J133.2, J134.SHLD1, J134.SHLD2, J134.SHLD3, J134.SHLD4, SHLD66.2
- new net SHLD67: J135.2, J136.SHLD1, J136.SHLD2, J136.SHLD3, J136.SHLD4, SHLD67.2
- new net SHLD68: J137.2, J138.SHLD1, J138.SHLD2, J138.SHLD3, J138.SHLD4, SHLD68.2
- new net SHLD69: J139.2, J140.SHLD1, J140.SHLD2, J140.SHLD3, J140.SHLD4, SHLD69.2
- new net VBUS20: J41.7, J42.A4, J42.A9, J42.B4, J42.B9
- new net VBUS21: J43.7, J44.A4, J44.A9, J44.B4, J44.B9
- new net VBUS22: J45.7, J46.A4, J46.A9, J46.B4, J46.B9
- new net VBUS23: J47.7, J48.A4, J48.A9, J48.B4, J48.B9
- new net VBUS24: J49.7, J50.A4, J50.A9, J50.B4, J50.B9
- new net VBUS25: J51.7, J52.A4, J52.A9, J52.B4, J52.B9
- new net VBUS26: J53.7, J54.A4, J54.A9, J54.B4, J54.B9
- new net VBUS27: J55.7, J56.A4, J56.A9, J56.B4, J56.B9
- new net VBUS28: J57.7, J58.A4, J58.A9, J58.B4, J58.B9
- new net VBUS29: J59.7, J60.A4, J60.A9, J60.B4, J60.B9
- new net VBUS30: J61.7, J62.A4, J62.A9, J62.B4, J62.B9
- new net VBUS31: J63.7, J64.A4, J64.A9, J64.B4, J64.B9
- new net VBUS32: J65.7, J66.A4, J66.A9, J66.B4, J66.B9
- new net VBUS33: J67.7, J68.A4, J68.A9, J68.B4, J68.B9
- new net VBUS34: J69.7, J70.A4, J70.A9, J70.B4, J70.B9
- new net VBUS35: J71.7, J72.A4, J72.A9, J72.B4, J72.B9
- new net VBUS36: J73.7, J74.A4, J74.A9, J74.B4, J74.B9
- new net VBUS37: J75.7, J76.A4, J76.A9, J76.B4, J76.B9
- new net VBUS38: J77.7, J78.A4, J78.A9, J78.B4, J78.B9
- new net VBUS39: J79.7, J80.A4, J80.A9, J80.B4, J80.B9
- new net VBUS40: J81.7, J82.A4, J82.A9, J82.B4, J82.B9
- new net VBUS41: J83.7, J84.A4, J84.A9, J84.B4, J84.B9
- new net VBUS42: J85.7, J86.A4, J86.A9, J86.B4, J86.B9
- new net VBUS43: J87.7, J88.A4, J88.A9, J88.B4, J88.B9
- new net VBUS44: J89.7, J90.A4, J90.A9, J90.B4, J90.B9
- new net VBUS45: J91.7, J92.A4, J92.A9, J92.B4, J92.B9
- new net VBUS46: J93.7, J94.A4, J94.A9, J94.B4, J94.B9
- new net VBUS47: J95.7, J96.A4, J96.A9, J96.B4, J96.B9
- new net VBUS48: J97.7, J98.A4, J98.A9, J98.B4, J98.B9
- new net VBUS49: J100.A4, J100.A9, J100.B4, J100.B9, J99.7
- new net VBUS50: J101.7, J102.A4, J102.A9, J102.B4, J102.B9
- new net VBUS51: J103.7, J104.A4, J104.A9, J104.B4, J104.B9
- new net VBUS52: J105.7, J106.A4, J106.A9, J106.B4, J106.B9
- new net VBUS53: J107.7, J108.A4, J108.A9, J108.B4, J108.B9
- new net VBUS54: J109.7, J110.A4, J110.A9, J110.B4, J110.B9
- new net VBUS55: J111.7, J112.A4, J112.A9, J112.B4, J112.B9
- new net VBUS56: J113.7, J114.A4, J114.A9, J114.B4, J114.B9
- new net VBUS57: J115.7, J116.A4, J116.A9, J116.B4, J116.B9
- new net VBUS58: J117.7, J118.A4, J118.A9, J118.B4, J118.B9
- new net VBUS59: J119.7, J120.A4, J120.A9, J120.B4, J120.B9
- new net VBUS60: J121.7, J122.A4, J122.A9, J122.B4, J122.B9
- new net VBUS61: J123.7, J124.A4, J124.A9, J124.B4, J124.B9
- new net VBUS62: J125.7, J126.A4, J126.A9, J126.B4, J126.B9
- new net VBUS63: J127.7, J128.A4, J128.A9, J128.B4, J128.B9
- new net VBUS64: J129.7, J130.A4, J130.A9, J130.B4, J130.B9
- new net VBUS65: J131.7, J132.A4, J132.A9, J132.B4, J132.B9
- new net VBUS66: J133.7, J134.A4, J134.A9, J134.B4, J134.B9
- new net VBUS67: J135.7, J136.A4, J136.A9, J136.B4, J136.B9
- new net VBUS68: J137.7, J138.A4, J138.A9, J138.B4, J138.B9
- new net VBUS69: J139.7, J140.A4, J140.A9, J140.B4, J140.B9
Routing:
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- added copper zone on layer 1, net GND20
- added copper zone on layer 16, net GND20
- added copper zone on layer 1, net GND21
- added copper zone on layer 16, net GND21
- added copper zone on layer 1, net GND22
- added copper zone on layer 16, net GND22
- added copper zone on layer 1, net GND23
- added copper zone on layer 16, net GND23
- added copper zone on layer 1, net GND24
- added copper zone on layer 16, net GND24
- added copper zone on layer 1, net GND25
- added copper zone on layer 16, net GND25
- added copper zone on layer 1, net GND26
- added copper zone on layer 16, net GND26
- added copper zone on layer 1, net GND27
- added copper zone on layer 16, net GND27
- added copper zone on layer 1, net GND28
- added copper zone on layer 16, net GND28
- added copper zone on layer 1, net GND29
- added copper zone on layer 16, net GND29
- added copper zone on layer 1, net GND30
- added copper zone on layer 16, net GND30
- added copper zone on layer 1, net GND31
- added copper zone on layer 16, net GND31
- added copper zone on layer 1, net GND32
- added copper zone on layer 16, net GND32
- added copper zone on layer 1, net GND33
- added copper zone on layer 16, net GND33
- added copper zone on layer 1, net GND34
- added copper zone on layer 16, net GND34
- added copper zone on layer 1, net GND35
- added copper zone on layer 16, net GND35
- added copper zone on layer 1, net GND36
- added copper zone on layer 16, net GND36
- added copper zone on layer 1, net GND37
- added copper zone on layer 16, net GND37
- added copper zone on layer 1, net GND38
- added copper zone on layer 16, net GND38
- added copper zone on layer 1, net GND39
- added copper zone on layer 16, net GND39
- added copper zone on layer 1, net GND40
- added copper zone on layer 16, net GND40
- added copper zone on layer 1, net GND41
- added copper zone on layer 16, net GND41
- added copper zone on layer 1, net GND42
- added copper zone on layer 16, net GND42
- added copper zone on layer 1, net GND43
- added copper zone on layer 16, net GND43
- added copper zone on layer 1, net GND44
- added copper zone on layer 16, net GND44
- added copper zone on layer 1, net GND45
- added copper zone on layer 16, net GND45
- added copper zone on layer 1, net GND46
- added copper zone on layer 16, net GND46
- added copper zone on layer 1, net GND47
- added copper zone on layer 16, net GND47
- added copper zone on layer 1, net GND48
- added copper zone on layer 16, net GND48
- added copper zone on layer 1, net GND49
- added copper zone on layer 16, net GND49
- added copper zone on layer 1, net GND50
- added copper zone on layer 16, net GND50
- added copper zone on layer 1, net GND51
- added copper zone on layer 16, net GND51
- added copper zone on layer 1, net GND52
- added copper zone on layer 16, net GND52
- added copper zone on layer 1, net GND53
- added copper zone on layer 16, net GND53
- added copper zone on layer 1, net GND54
- added copper zone on layer 16, net GND54
- added copper zone on layer 1, net GND55
- added copper zone on layer 16, net GND55
- added copper zone on layer 1, net GND56
- added copper zone on layer 16, net GND56
- added copper zone on layer 1, net GND57
- added copper zone on layer 16, net GND57
- added copper zone on layer 1, net GND58
- added copper zone on layer 16, net GND58
- added copper zone on layer 1, net GND59
- added copper zone on layer 16, net GND59
- added copper zone on layer 1, net GND60
- added copper zone on layer 16, net GND60
- added copper zone on layer 1, net GND61
- added copper zone on layer 16, net GND61
- added copper zone on layer 1, net GND62
- added copper zone on layer 16, net GND62
- added copper zone on layer 1, net GND63
- added copper zone on layer 16, net GND63
- added copper zone on layer 1, net GND64
- added copper zone on layer 16, net GND64
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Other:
- board size 106.7 x 103.4 mm -> 189.2 x 165.9 mm
